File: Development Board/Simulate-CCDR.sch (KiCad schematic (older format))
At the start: 19 parts

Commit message: main sheets created
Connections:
- net labels added: UART_RX, UART_TX, USB_D+, USB_D-
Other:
- moved on the sheet: H?, J?, Q?, Q?A, Q?B, R?, U?

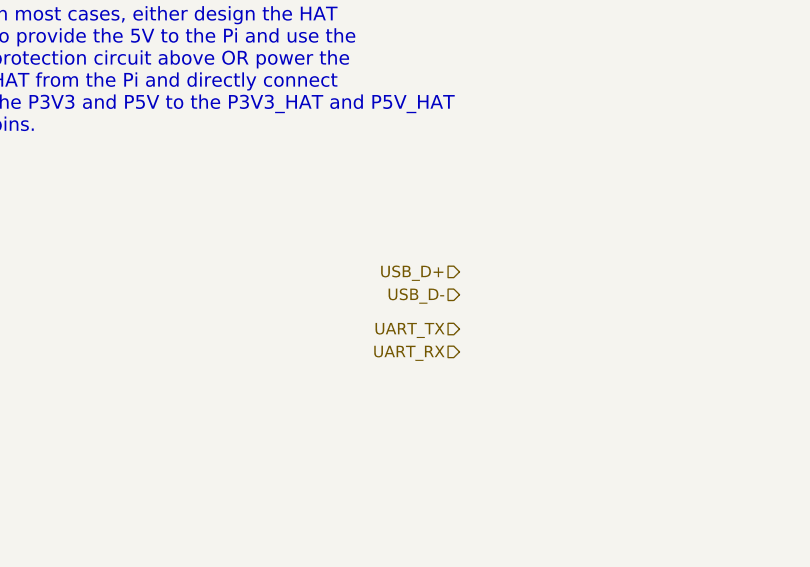
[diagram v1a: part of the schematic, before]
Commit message: added FTDI
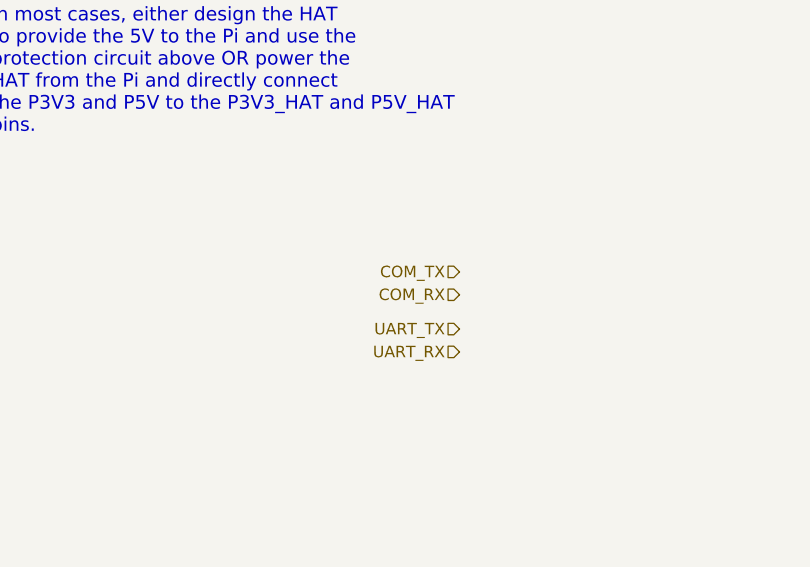
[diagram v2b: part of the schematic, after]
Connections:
- net labels added: COM_RX, COM_TX
- net labels removed: USB_D+, USB_D-
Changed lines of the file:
@@
 $Descr A4 11693 8268
 encoding utf-8
-Sheet 2 9
+Sheet 2 10
 Title ""
 Date ""
@@
 	2050 5800 2150 5800
 Text HLabel 10200 5250 0    50   Input ~ 0
-USB_D+
+COM_TX
 Text HLabel 10200 5350 0    50   Input ~ 0
-USB_D-
+COM_RX
 Text HLabel 10200 5500 0    50   Input ~ 0
 UART_TX

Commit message: added KISS description, UART-I2C chip
keep it simple, stupid. Goal is to create software development board for sub-system comms
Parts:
- removed J?: CONN_02X02, Connector_PinHeader_2.54mm:PinHeader_2x02_P2.54mm_Vertical, symbol Connector_Generic:Conn_02x02_Odd_Even
- removed J?: CONN_01X02, Connector_PinHeader_2.54mm:PinHeader_1x02_P2.54mm_Vertical, symbol Connector_Generic:Conn_01x02
- removed Q?: DMG2305UX, Package_TO_SOT_SMD:SOT-23, symbol QPACE-DevelopmentBoard-rescue:DMG2305UX-raspberrypi_hat
- removed Q? (x2): DMMT5401, Package_TO_SOT_SMD:SOT-23-6, symbol QPACE-DevelopmentBoard-rescue:DMMT5401-raspberrypi_hat
- removed R? (x2): 10K, Resistor_SMD:R_0603_1608Metric_Pad0.84x1.00mm_HandSolder, symbol Device:R
- removed R?: 47K, Resistor_SMD:R_0603_1608Metric_Pad0.84x1.00mm_HandSolder, symbol Device:R
- removed R? (x2): 3.9K, Resistor_SMD:R_0603_1608Metric_Pad0.84x1.00mm_HandSolder, symbol Device:R
- removed R? (x3): DNP, Resistor_SMD:R_0603_1608Metric_Pad0.84x1.00mm_HandSolder, symbol Device:R
- removed U?: CAT24C32, Package_SOIC:SOIC-8_3.9x4.9mm_P1.27mm, symbol QPACE-DevelopmentBoard-rescue:CAT24C32-raspberrypi_hat
- added C?: 0.1uF, symbol device:C
- added C? (x2): 18pF, symbol device:C
- added R?: 1k, symbol device:R
- added R?: 10k, symbol device:R
- added R?: 10K, symbol device:R
- added U?: SC16IS740, symbol QPACE-SchematicSymbols:SC16IS740
- added Y?: 1.8432MHz, symbol device:Crystal
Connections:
- net labels added: +3.3V
- net labels removed: ID_SC_EEPROM_pu, ID_SD_EEPROM_pu, P3V3, P5V
- wire segments 82 -> 52
- no-connect marks 0 -> 3
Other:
- note added: "determine where the ~IRQ, SDA, SCL connect to the RPi at."
- note removed: "5V Powered HAT Protection"
- note removed: "EEPROM WRITE ENABLE"
- note removed: "FLEXIBLE POWER SELECTION"
- note removed: "HAT EEPROM"
- note removed: "HAT spec indicates to NEVER\npower the 3.3V pins on the Raspberry Pi \nfrom the HAT header. Only connect the 3.3V\npower from the Pi if the HAT does not have\n3.3V on board.\n\nIF you are designing a board that could\neither be powered by the Pi or from the HAT\nthe jumpers here can be used.\n\nIn most cases, either design the HAT \nto provide the 5V to the Pi and use the\nprotection circuit abov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"
- note removed: "Pullup Resistors"
- note removed: "The HAT spec requires this EEPROM with system information\nto be in place in order to be called a HAT. It should be set up as write\nprotected (WP pin held high), so it may be desirable to either put a \njumper as shown to enable writing, or to hook up a spare IO pin to do so."
- note removed: "These are just pullup resistors for the I2C bus on the EEPROM.\nThe resistor values are per the HAT spec."
- note removed: "This is based on the official Raspberry Pi spec to be able to call an extension board a HAT.\nhttps://github.com/raspberrypi/hats/blob/master/designguide.md"
- note removed: "This is the recommended 5V rail protection for \na HAT with power going to the Pi.\nSee https://github.com/raspberrypi/hats/blob/master/designguide.md#back-powering-the-pi-via-the-j8-gpio-header"
- moved on the sheet: H?, J?

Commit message: reduced complexity
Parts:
- added Q?: BSS138, Package_TO_SOT_SMD:SOT-23, symbol Transistor_FET:BSS138
- added Q?: Q_PMOS_GDSD, symbol device:Q_PMOS_GDSD
- added R? (x2): R, symbol device:R
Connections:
- net labels added: +5V, EN_PiPwr, Pi_I2C_SCL, Pi_I2C_SDA, Pi_I2C_~IRQ
- wire segments 52 -> 66
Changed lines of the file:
@@
 $Descr A4 11693 8268
 encoding utf-8
-Sheet 2 12
+Sheet 2 13
 Title ""
 Date ""
@@
 Text Notes 5100 3900 0    50   ~ 0
 determine where the ~IRQ, SDA, SCL connect to the RPi at.
+$Comp
+L Transistor_FET:BSS138 Q?
+U 1 1 5C96F9A5
+P 4200 5300
+F 0 "Q?" H 4405 5346 50  0000 L CNN
+F 1 "BSS138" H 4405 5255 50  0000 L CNN
+F 2 "Package_TO_SOT_SMD:SOT-23" H 4400 5225 50  0001 L CIN
+F 3 "https://www.fairchildsemi.com/datasheets/BS/BSS138.pdf" H 4200 5300 50  0001 L CNN
+	1    4200 5300
+	1    0    0    -1
+$EndComp
+$Comp
+L device:Q_PMOS_GDSD Q?
+U 1 1 5C9700AA
+P 4300 4600
+F 0 "Q?" V 4725 4600 50  0000 C CNN
+F 1 "Q_PMOS_GDSD" V 4634 4600 50  0000 C CNN
+F 2 "" H 4500 4700 50  0001 C CNN
+F 3 "~" H 4300 4600 50  0001 C CNN
+	1    4300 4600
+	0    1    -1   0
+$EndComp
+$Comp
+L device:R R?
+U 1 1 5C9726D0
+P 3800 5450
+F 0 "R?" H 3870 5496 50  0000 L CNN
+F 1 "R" H 3870 5405 50  0000 L CNN
+F 2 "" V 3730 5450 50  0001 C CNN
+F 3 "~" H 3800 5450 50  0001 C CNN
+	1    3800 5450
+	1    0    0    -1
+$EndComp
+$Comp
+L power:GND #PWR?
+U 1 1 5C97274E
+P 4300 5600
+F 0 "#PWR?" H 4300 5350 50  0001 C CNN
+F 1 "GND" H 4300 5450 50  0000 C CNN
+F 2 "" H 4300 5600 50  0000 C CNN
+F 3 "" H 4300 5600 50  0000 C CNN
+	1    4300 5600
+	1    0    0    -1
+$EndComp
+Wire Wire Line
+	4300 5500 4300 5600
+Wire Wire Line
+	4300 5600 3800 5600
+Connection ~ 4300 5600
+Wire Wire Line
+	3800 5300 4000 5300
+$Comp
+L device:R R?
+U 1 1 5C974A04
+P 3900 4650
+F 0 "R?" H 3970 4696 50  0000 L CNN
+F 1 "R" H 3970 4605 50  0000 L CNN
+F 2 "" V 3830 4650 50  0001 C CNN
+F 3 "~" H 3900 4650 50  0001 C CNN
+	1    3900 4650
+	1    0    0    -1
+$EndComp
+Wire Wire Line
+	3900 4500 4100 4500
+Wire Wire Line
+	3900 4800 3900 4900
+Wire Wire Line
+	3900 4900 4300 4900
+Wire Wire Line
+	4300 4900 4300 4800
+Wire Wire Line
+	4300 5100 4300 4900
+Connection ~ 4300 4900
+Wire Wire Line
+	4500 4400 4700 4400
+Wire Wire Line
+	4700 4400 4700 4500
+Wire Wire Line
+	4700 4500 4500 4500
+Wire Wire Line
+	4700 4500 4900 4500
+Connection ~ 4700 4500
+Wire Wire Line
+	3900 4500 3500 4500
+Connection ~ 3900 4500
+$Comp
+L power:+5V #PWR?
+U 1 1 5C97B93E
+P 3500 4500
+F 0 "#PWR?" H 3500 4350 50  0001 C CNN
+F 1 "+5V" H 3515 4673 50  0000 C CNN
+F 2 "" H 3500 4500 50  0001 C CNN
+F 3 "" H 3500 4500 50  0001 C CNN
+	1    3500 4500
+	1    0    0    -1
+$EndComp
+Text Label 4900 4500 0    60   ~ 0
+P5V_HAT
+Wire Wire Line
+	3800 5300 3400 5300
+Connection ~ 3800 5300
+Text HLabel 3400 5300 0    50   Input ~ 0
+EN_PiPwr
+$Comp
+L power:GND #PWR?
+U 1 1 5C99F5E0
+P 2050 3600
+F 0 "#PWR?" H 2050 3350 50  0001 C CNN
+F 1 "GND" H 2050 3450 50  0000 C CNN
+F 2 "" H 2050 3600 50  0000 C CNN
+F 3 "" H 2050 3600 50  0000 C CNN
+	1    2050 3600
+	1    0    0    -1
+$EndComp
+Connection ~ 2050 3600
+Text Label 2050 1800 2    50   ~ 0
+Pi_I2C_SDA
+Text Label 2050 1900 2    50   ~ 0
+Pi_I2C_SCL
+Text Label 5900 3600 0    50   ~ 0
+Pi_I2C_SCL
+Text Label 5900 3700 0    50   ~ 0
+Pi_I2C_SDA
+Text Label 5900 3400 0    50   ~ 0
+Pi_I2C_~IRQ
+Text Label 3250 3400 0    50   ~ 0
+Pi_I2C_~IRQ
 $EndSCHEMATC

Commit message: Q-PACE Devboard V0
This should complete the KiCad Schematic and PCB files. Parts should be in FSI inventory.
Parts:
- added J11: Pi_I2C-BUS, Socket_Strips:Socket_Strip_Straight_1x03_Pitch2.54mm, symbol Connector_Generic:Conn_01x03
- added TP5, TP6, TP7: TestPoint, Measurement_Points:Measurement_Point_Round-SMD-Pad_Small, symbol Connector:TestPoint
- C3, C4, C5: renamed from C?; footprint (none) -> Capacitors_SMD:C_0805; symbol device:C -> QPACE-DevelopmentBoard-rescue:C-device
- Q1: renamed from Q?; footprint Package_TO_SOT_SMD:SOT-23 -> TO_SOT_Packages_SMD:SOT-23
- Q2: renamed from Q?; footprint (none) -> TO_SOT_Packages_SMD:SOT-223; symbol device:Q_PMOS_GDSD -> QPACE-DevelopmentBoard-rescue:Q_PMOS_GDSD-device
- R4, R5: renamed from R?; value R -> 100k; footprint (none) -> Resistors_SMD:R_0805; symbol device:R -> QPACE-DevelopmentBoard-rescue:R-device
- R6, R7, R8: renamed from R?; footprint (none) -> Resistors_SMD:R_0805; symbol device:R -> QPACE-DevelopmentBoard-rescue:R-device
- U2: renamed from U?; footprint (none) -> Housings_SSOP:TSSOP-16-1EP_4.4x5mm_Pitch0.65mm; symbol QPACE-SchematicSymbols:SC16IS740 -> QPACE-DevelopmentBoard-rescue:SC16IS740-QPACE-SchematicSymbols
- Y1: renamed from Y?; footprint (none) -> Crystals:Crystal_HC49-U_Vertical; symbol device:Crystal -> QPACE-DevelopmentBoard-rescue:Crystal-device
- gave numbers to parts that had none: 5
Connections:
- net EN_PiPwr: now also TP5.1
- net GND: now also J11.3 (Pin_3)
- net P5V_HAT: now also TP6.1
- net Pi_I2C_SCL: now also J11.1 (Pin_1)
- net Pi_I2C_SDA: now also J11.2 (Pin_2)
- net Pi_I2C_~IRQ: now also TP7.1
- no-connect marks 3 -> 25

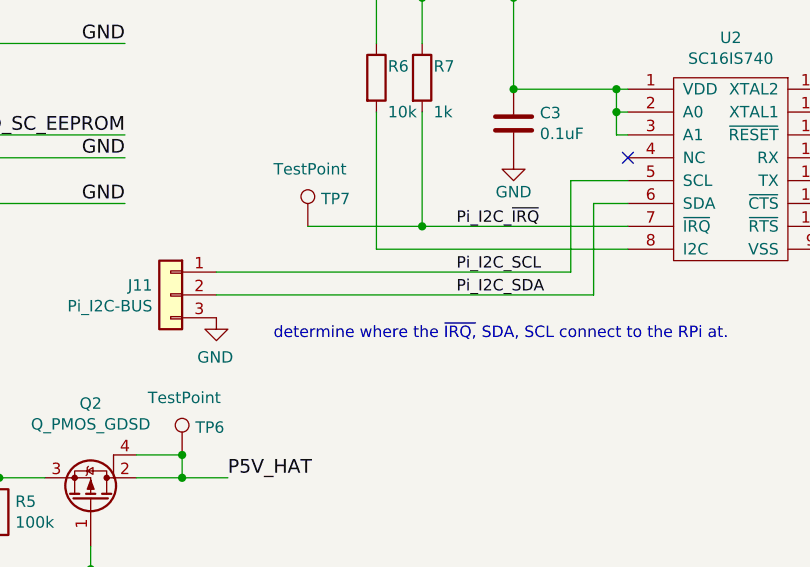
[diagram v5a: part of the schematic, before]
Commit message: added silk screen, organized pins
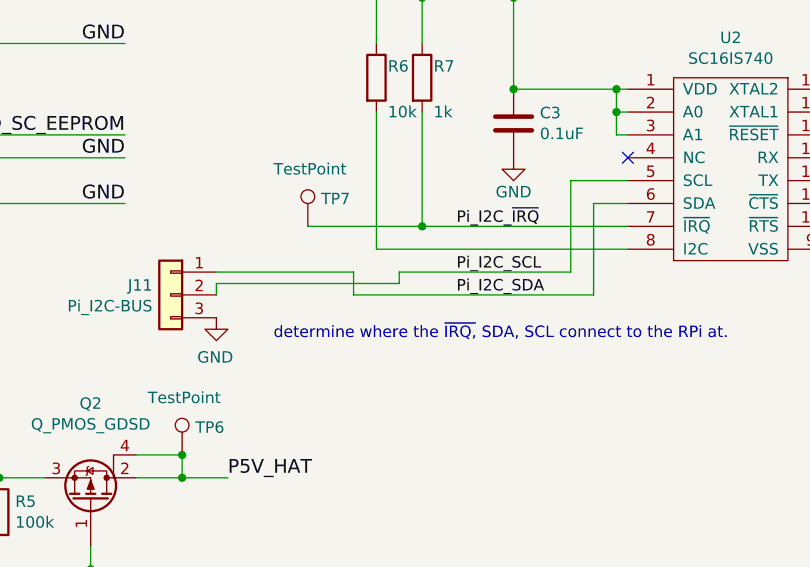
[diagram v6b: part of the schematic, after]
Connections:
- net Pi_I2C_SCL: now also J11.2 (Pin_2); no longer J11.1 (Pin_1)
- net Pi_I2C_SDA: now also J11.1 (Pin_1); no longer J11.2 (Pin_2)
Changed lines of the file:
@@
 $EndComp
 Wire Wire Line
-	4850 3600 6400 3600
+	4850 3600 5450 3600
 Wire Wire Line
-	4850 3700 6500 3700
+	5450 3600 5450 3700
+Wire Wire Line
+	5450 3700 6500 3700
+Wire Wire Line
+	5650 3600 5650 3650
+Wire Wire Line
+	5650 3650 4850 3650
+Wire Wire Line
+	4850 3650 4850 3700
+Wire Wire Line
+	5650 3600 6400 3600
 $EndSCHEMATC

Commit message: ready for production
passed all KiCad error checking. schematic and pcblayout were both validated. ready to be ordered
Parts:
- removed J11: Pi_I2C-BUS, Socket_Strips:Socket_Strip_Straight_1x03_Pitch2.54mm, symbol Connector_Generic:Conn_01x03
- added TP15, TP16: TestPoint, Measurement_Points:Measurement_Point_Round-SMD-Pad_Small, symbol Connector:TestPoint
- renumbered J14 to J13, TP5 to TP13, TP6 to TP14, TP7 to TP17
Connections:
- net Pi_I2C_SCL: now also TP16.1
- net Pi_I2C_SDA: now also TP15.1
- net PiHeartBeat: now reaches J13.12 (BCM18)
- net P3V3_HAT: no longer names the net of J13.1 (P3V3)
- no-connect marks 25 -> 27
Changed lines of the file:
@@
 encoding utf-8
 Sheet 2 3
-Title ""
-Date ""
-Rev ""
-Comp ""
-Comment1 ""
-Comment2 ""
-Comment3 ""
-Comment4 ""
+Title "Q-PACE Development Board Raspberry Pi Hat"
+Date "2019-04-29"
+Rev "R0"
+Comp "FSI"
+Comment1 "created by Theodore Cox (TCC)"
+Comment2 "The simulated boards include; the WTC (STM32), CCDR (R Pi) and RF (EnduroSat)"
+Comment3 "This should connect to a Raspberry Pi with other necessary connections"
+Comment4 "This device is to be used to develop code for Q-PACE"
 $EndDescr
 $Comp
@@
 $EndComp
 $Comp
-L QPACE-DevelopmentBoard-rescue:OX40HAT-raspberrypi_hat J14
+L QPACE-DevelopmentBoard-rescue:OX40HAT-raspberrypi_hat J13
 U 1 1 5C7F637C
 P 2650 1700
-F 0 "J14" H 3000 1800 50  0000 C CNN
+F 0 "J13" H 3000 1800 50  0000 C CNN
 F 1 "40HAT" H 2350 1800 50  0000 C CNN
 F 2 "Connector_PinSocket_2.54mm:PinSocket_2x20_P2.54mm_Vertical" H 2650 1900 50  0001 C CNN
@@
 Text Notes 1700 1450 0    118  ~ 24
 40-Pin HAT Connector
-Text Label 850  3600 0    60   ~ 0
-GND
-Wire Wire Line
-	2050 3600 850  3600
 Text Label 850  3000 0    60   ~ 0
 ID_SD_EEPROM
 Wire Wire Line
 	2050 3000 850  3000
-Text Label 850  2900 0    60   ~ 0
-GND
-Wire Wire Line
-	2050 2900 850  2900
-Text Label 850  2100 0    60   ~ 0
-GND
-Wire Wire Line
-	2050 2100 850  2100
-Text Label 850  1700 0    60   ~ 0
-P3V3_HAT
-Wire Wire Line
-	2050 1700 850  1700
-Wire Wire Line
-	3250 2300 4450 2300
-Wire Wire Line
-	3250 2600 4450 2600
+Wire Wire Line
+	2050 2900 2000 2900
+Wire Wire Line
+	2050 2100 1950 2100
+Wire Wire Line
+	3250 2300 3400 2300
+Wire Wire Line
+	3250 2600 3400 2600
 Wire Wire Line
 	3250 3000 4450 3000
@@
 Wire Wire Line
 	3250 3300 4450 3300
-Text Label 4450 2300 2    60   ~ 0
-GND
-Text Label 4450 2600 2    60   ~ 0
-GND
 Text Label 4450 3100 2    60   ~ 0
 GND
@@
 Text Label 4450 3300 2    60   ~ 0
 GND
-Text Label 4450 1900 2    60   ~ 0
-GND
-Wire Wire Line
-	3250 1900 4450 1900
+Wire Wire Line
+	3250 1900 3400 1900
 Text Label 4450 1800 2    60   ~ 0
 P5V_HAT
@@
 	8150 2900 8000 2900
 $Comp
-L power:GND #PWR0127
+L power:GND #PWR034
 U 1 1 5C8CE47C
 P 7550 3500
-F 0 "#PWR0127" H 7550 3250 50  0001 C CNN
+F 0 "#PWR034" H 7550 3250 50  0001 C CNN
 F 1 "GND" H 7550 3350 50  0000 C CNN
 F 2 "" H 7550 3500 50  0000 C CNN
@@
 	8450 2900 8550 2900
 $Comp
-L power:GND #PWR0128
+L power:GND #PWR035
 U 1 1 5C8D90CD
 P 8000 3200
-F 0 "#PWR0128" H 8000 2950 50  0001 C CNN
+F 0 "#PWR035" H 8000 2950 50  0001 C CNN
 F 1 "GND" H 8000 3050 50  0000 C CNN
 F 2 "" H 8000 3200 50  0000 C CNN
@@
 	7750 3000 7750 2700
 $Comp
-L power:+3.3V #PWR0129
+L power:+3.3V #PWR032
 U 1 1 5C8DACCC
 P 6150 2300
-F 0 "#PWR0129" H 6150 2150 50  0001 C CNN
+F 0 "#PWR032" H 6150 2150 50  0001 C CNN
 F 1 "+3.3V" H 6165 2473 50  0000 C CNN
 F 2 "" H 6150 2300 50  0001 C CNN
@@
 	6150 2400 6150 2800
 $Comp
-L power:GND #PWR0130
+L power:GND #PWR033
 U 1 1 5C8DB92B
 P 6150 3100
-F 0 "#PWR0130" H 6150 2850 50  0001 C CNN
+F 0 "#PWR033" H 6150 2850 50  0001 C CNN
 F 1 "GND" H 6150 2950 50  0000 C CNN
 F 2 "" H 6150 3100 50  0000 C CNN
@@
 $EndComp
 $Comp
-L power:GND #PWR0131
+L power:GND #PWR031
 U 1 1 5C97274E
 P 4300 5600
-F 0 "#PWR0131" H 4300 5350 50  0001 C CNN
+F 0 "#PWR031" H 4300 5350 50  0001 C CNN
 F 1 "GND" H 4300 5450 50  0000 C CNN
 F 2 "" H 4300 5600 50  0000 C CNN
@@
 Connection ~ 3900 4500
 $Comp
-L power:+5V #PWR0132
+L power:+5V #PWR030
 U 1 1 5C97B93E
 P 3500 4500
-F 0 "#PWR0132" H 3500 4350 50  0001 C CNN
+F 0 "#PWR030" H 3500 4350 50  0001 C CNN
 F 1 "+5V" H 3515 4673 50  0000 C CNN
 F 2 "" H 3500 4500 50  0001 C CNN
@@
 EN_PiPwr
 $Comp
-L power:GND #PWR0133
+L power:GND #PWR029
 U 1 1 5C99F5E0
-P 2050 3600
-F 0 "#PWR0133" H 2050 3350 50  0001 C CNN
-F 1 "GND" H 2050 3450 50  0000 C CNN
-F 2 "" H 2050 3600 50  0000 C CNN
-F 3 "" H 2050 3600 50  0000 C CNN
-	1    2050 3600
-	1    0    0    -1
-$EndComp
-Connection ~ 2050 3600
+P 1900 3600
+F 0 "#PWR029" H 1900 3350 50  0001 C CNN
+F 1 "GND" H 1900 3450 50  0000 C CNN
+F 2 "" H 1900 3600 50  0000 C CNN
+F 3 "" H 1900 3600 50  0000 C CNN
+	1    1900 3600
+	0    1    1    0
+$EndComp
 Text Label 2050 1800 2    50   ~ 0
 Pi_I2C_SDA
@@
 NoConn ~ 3250 2500
 NoConn ~ 3250 2400
-NoConn ~ 3250 2200
 NoConn ~ 2050 2700
 $Comp
-L Connector:TestPoint TP5
+L Connector:TestPoint TP13
 U 1 1 5CD23D6C
 P 3800 5300
-F 0 "TP5" H 3858 5420 50  0000 L CNN
+F 0 "TP13" H 3858 5420 50  0000 L CNN
 F 1 "TestPoint" H 3350 5400 50  0000 L CNN
 F 2 "Measurement_Points:Measurement_Point_Round-SMD-Pad_Small" H 4000 5300 50  0001 C CNN
@@
 $EndComp
 $Comp
-L Connector:TestPoint TP6
+L Connector:TestPoint TP14
 U 1 1 5CD23ED0
 P 4700 4400
-F 0 "TP6" H 4758 4520 50  0000 L CNN
+F 0 "TP14" H 4758 4520 50  0000 L CNN
 F 1 "TestPoint" H 4550 4650 50  0000 L CNN
 F 2 "Measurement_Points:Measurement_Point_Round-SMD-Pad_Small" H 4900 4400 50  0001 C CNN
@@
 Connection ~ 4700 4400
 $Comp
-L Connector:TestPoint TP7
+L Connector:TestPoint TP17
 U 1 1 5CD240D9
 P 5250 3400
-F 0 "TP7" H 5308 3520 50  0000 L CNN
+F 0 "TP17" H 5308 3520 50  0000 L CNN
 F 1 "TestPoint" H 5100 3650 50  0000 L CNN
 F 2 "Measurement_Points:Measurement_Point_Round-SMD-Pad_Small" H 5450 3400 50  0001 C CNN
@@
 	5250 3400 5750 3400
 Connection ~ 5750 3400
-$Comp
-L Connector_Generic:Conn_01x03 J?
-U 1 1 5CD263C3
-P 4650 3700
-AR Path="/5CD263C3" Ref="J?"  Part="1"
-AR Path="/5C7F607C/5CD263C3" Ref="J11"  Part="1"
-F 0 "J11" H 4730 3742 50  0000 L CNN
-F 1 "Pi_I2C-BUS" H 4730 3651 50  0000 L CNN
-F 2 "Socket_Strips:Socket_Strip_Straight_1x03_Pitch2.54mm" H 4650 3700 50  0001 C CNN
-F 3 "~" H 4650 3700 50  0001 C CNN
-	1    4650 3700
-	-1   0    0    -1
-$EndComp
-$Comp
-L power:GND #PWR?
-U 1 1 5CD263CA
-P 4850 3800
-AR Path="/5CD263CA" Ref="#PWR?"  Part="1"
-AR Path="/5C7F607C/5CD263CA" Ref="#PWR0136"  Part="1"
-F 0 "#PWR0136" H 4850 3550 50  0001 C CNN
-F 1 "GND" H 4855 3627 50  0000 C CNN
-F 2 "" H 4850 3800 50  0001 C CNN
-F 3 "" H 4850 3800 50  0001 C CNN
-	1    4850 3800
-	-1   0    0    -1
-$EndComp
-Wire Wire Line
-	4850 3600 5450 3600
-Wire Wire Line
-	5450 3600 5450 3700
-Wire Wire Line
-	5450 3700 6500 3700
-Wire Wire Line
-	5650 3600 5650 3650
-Wire Wire Line
-	5650 3650 4850 3650
-Wire Wire Line
-	4850 3650 4850 3700
-Wire Wire Line
-	5650 3600 6400 3600
+NoConn ~ 2050 1700
+Wire Wire Line
+	3250 2200 4450 2200
+Text HLabel 4450 2200 2    50   Input ~ 0
+PiHeartBeat
+$Comp
+L Connector:TestPoint TP16
+U 1 1 5CCCEF95
+P 5050 3600
+F 0 "TP16" H 5100 3650 50  0000 L CNN
+F 1 "TestPoint" H 4850 3800 50  0000 L CNN
+F 2 "Measurement_Points:Measurement_Point_Round-SMD-Pad_Small" H 5250 3600 50  0001 C CNN
+F 3 "~" H 5250 3600 50  0001 C CNN
+	1    5050 3600
+	1    0    0    -1
+$EndComp
+$Comp
+L Connector:TestPoint TP15
+U 1 1 5CCCF15F
+P 4850 3700
+F 0 "TP15" H 4900 3750 50  0000 L CNN
+F 1 "TestPoint" H 4700 3650 50  0000 L CNN
+F 2 "Measurement_Points:Measurement_Point_Round-SMD-Pad_Small" H 5050 3700 50  0001 C CNN
+F 3 "~" H 5050 3700 50  0001 C CNN
+	1    4850 3700
+	1    0    0    -1
+$EndComp
+Wire Wire Line
+	4850 3700 6500 3700
+Wire Wire Line
+	5050 3600 6400 3600
+NoConn ~ 2050 3000
+NoConn ~ 3250 3000
+Wire Wire Line
+	2050 3600 1900 3600
+$Comp
+L power:GND #PWR0101
+U 1 1 5CC9A58F
+P 2000 2900
+F 0 "#PWR0101" H 2000 2650 50  0001 C CNN
+F 1 "GND" H 2000 2750 50  0000 C CNN
+F 2 "" H 2000 2900 50  0000 C CNN
+F 3 "" H 2000 2900 50  0000 C CNN
+	1    2000 2900
+	0    1    1    0
+$EndComp
+$Comp
+L power:GND #PWR0102
+U 1 1 5CC9EC28
+P 1950 2100
+F 0 "#PWR0102" H 1950 1850 50  0001 C CNN
+F 1 "GND" H 1950 1950 50  0000 C CNN
+F 2 "" H 1950 2100 50  0000 C CNN
+F 3 "" H 1950 2100 50  0000 C CNN
+	1    1950 2100
+	0    1    1    0
+$EndComp
+$Comp
+L power:GND #PWR0103
+U 1 1 5CCA0514
+P 3400 2600
+F 0 "#PWR0103" H 3400 2350 50  0001 C CNN
+F 1 "GND" H 3400 2450 50  0000 C CNN
+F 2 "" H 3400 2600 50  0000 C CNN
+F 3 "" H 3400 2600 50  0000 C CNN
+	1    3400 2600
+	0    -1   -1   0
+$EndComp
+$Comp
+L power:GND #PWR0104
+U 1 1 5CCA0630
+P 3400 2300
+F 0 "#PWR0104" H 3400 2050 50  0001 C CNN
+F 1 "GND" H 3400 2150 50  0000 C CNN
+F 2 "" H 3400 2300 50  0000 C CNN
+F 3 "" H 3400 2300 50  0000 C CNN
+	1    3400 2300
+	0    -1   -1   0
+$EndComp
+$Comp
+L power:GND #PWR0105
+U 1 1 5CCA06ED
+P 3400 1900
+F 0 "#PWR0105" H 3400 1650 50  0001 C CNN
+F 1 "GND" H 3400 1750 50  0000 C CNN
+F 2 "" H 3400 1900 50  0000 C CNN
+F 3 "" H 3400 1900 50  0000 C CNN
+	1    3400 1900
+	0    -1   -1   0
+$EndComp
+$Comp
+L power:GND #PWR0108
+U 1 1 5CCA64A4
+P 2300 4200
+F 0 "#PWR0108" H 2300 3950 50  0001 C CNN
+F 1 "GND" H 2300 4050 50  0000 C CNN
+F 2 "" H 2300 4200 50  0000 C CNN
+F 3 "" H 2300 4200 50  0000 C CNN
+	1    2300 4200
+	1    0    0    -1
+$EndComp
+Text HLabel 2300 4100 0    50   Input ~ 0
+GND
+Wire Wire Line
+	2300 4100 2300 4200
+$Comp
+L power:+3.3V #PWR0110
+U 1 1 5CD08F36
+P 6500 1450
+F 0 "#PWR0110" H 6500 1300 50  0001 C CNN
+F 1 "+3.3V" H 6515 1623 50  0000 C CNN
+F 2 "" H 6500 1450 50  0001 C CNN
+F 3 "" H 6500 1450 50  0001 C CNN
+	1    6500 1450
+	1    0    0    -1
+$EndComp
+Text HLabel 5950 1650 0    50   Input ~ 0
+3V3
+Wire Wire Line
+	5950 1650 6500 1650
+Wire Wire Line
+	6500 1650 6500 1450
 $EndSCHEMATC
